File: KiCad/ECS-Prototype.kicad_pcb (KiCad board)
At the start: 2 copper layers, 192.1 x 149.8 mm, 53 parts, among them J1 Connector1, J3 FC68131, J4 FC68131, J5 FC68131, Q1 PN2222A, T1 VB_05-1-12, T2 VB_05-1-12, T3 VB_05-1-12, U3 LT1498IN8, U4 MCP602T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

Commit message: modifications for pcb design: version 3
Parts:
- J3, J4, J5: value FC68131 -> SJ1-3515N; footprint DehneEVSEFootPrints:CLIFF_FC68131 -> ECS-PrototypeFootPrints:CUI_SJ1-3515N
- moved Ref** 1.91 mm to (310.8, 140.9)
- moved ? 1.45 mm to (210.1, 190.4)
- moved ? 1.45 mm to (310.3, 61.4)
- moved C1 1.45 mm to (271.0, 162.4)
- moved C2 1.45 mm to (271.0, 168.7)
- moved C3 1.45 mm to (251.8, 169.7)
- moved D1 1.45 mm to (222.1, 142.7)
- moved D2 1.45 mm to (243.6, 193.4)
- moved D3 1.45 mm to (240.6, 174.4)
- moved D4 1.45 mm to (197.6, 142.7)
- moved D5 1.45 mm to (173.3, 142.7)
- moved D6 1.45 mm to (270.3, 156.7)
- moved G*** 1.45 mm to (203.8, 84.2)
- moved J1 1.45 mm to (159.8, 170.9)
- moved L1 1.45 mm to (250.5, 158.9)
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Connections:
- J3 pad 2: Net-(J3-Pad2) -> CUR_SENS_L1
- J3 pad 5: CUR_SENS_L1 -> (no net)
- J4 pad 2: Net-(J4-Pad2) -> CUR_SENS_L2
- J4 pad 5: CUR_SENS_L2 -> (no net)
- J5 pad 2: Net-(J5-Pad2) -> CUR_SENS_L3
- J5 pad 5: CUR_SENS_L3 -> (no net)
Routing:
- net +5V: track 267.2 -> 348.0 mm, vias 1 -> 6
- net CP: track 184.7 -> 248.7 mm, vias 1 -> 3
- net CURRENT_SENS_L3_READ: track 163.4 -> 220.9 mm, vias 3 -> 4
- net PWM: track 91.2 -> 105.4 mm, vias 1 -> 2
- net VOLTAGE_SENS_L1_READ: track 108.7 -> 115.9 mm, vias 1 -> 2
- net CUR_SENS_L3: track 167.2 -> 173.9 mm
- net +12VDC: track 37.9 -> 44.3 mm, vias 0 -> 2
- net /PP: track 171.9 -> 178.1 mm, vias 2 -> 4
- net DC_RELAY: track 44.2 -> 49.2 mm, vias 1 -> 2
- net CURRENT_SENS_L2_READ: track 125.4 -> 130.3 mm
- net CUR_SENS_L1: track 86.2 -> 90.7 mm
- net +3V3: track 305.7 -> 301.4 mm, vias 1 -> 6
- net CUR_SENS_L2: track 121.7 -> 126.0 mm, vias 1 -> 2
- net Net-(D2-Pad2): track 43.2 -> 47.3 mm, vias 0 -> 2
- net VOLTAGE_SENS_L3_READ: track 193.6 -> 197.5 mm, vias 1 -> 2
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
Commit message: modifications for pcb design version 4: like v3 but with both faces soldering
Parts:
- moved C2 0.46 mm to (271.0, 168.2)
- moved R7 0.13 mm to (276.6, 147.5)
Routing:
- net +5V: track 348.0 -> 331.6 mm, vias 6 -> 1
- net +3V3: track 301.4 -> 317.2 mm, vias 6 -> 1
- net PWM: track 105.4 -> 94.7 mm, vias 2 -> 1
- net +12VDC: track 44.3 -> 38.1 mm, vias 2 -> 0
- net Net-(D2-Pad2): track 47.3 -> 43.8 mm, vias 2 -> 0
- net CUR_SENS_L2: track 126.0 -> 124.0 mm, vias 2 -> 1
- net DC_RELAY: track 49.2 -> 47.2 mm, vias 2 -> 1
- net Net-(R6-Pad2): track 16.3 -> 14.4 mm, vias 2 -> 0
- net CP: track 248.7 -> 246.8 mm, vias 3 -> 1
- net -12VDC: track 21.2 -> 19.7 mm
- net /PP: track 178.1 -> 176.8 mm, vias 4 -> 2
- net CUR_SENS_L3: track 173.9 -> 174.9 mm, vias 2 -> 1
- net MAINS_L1: track 90.6 -> 91.2 mm
- net CUR_SENS_L1: track 90.7 -> 90.6 mm, vias 2 -> 1
- net VOLTAGE_SENS_L3_READ: track 197.5 -> 197.4 mm, vias 2 -> 1
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
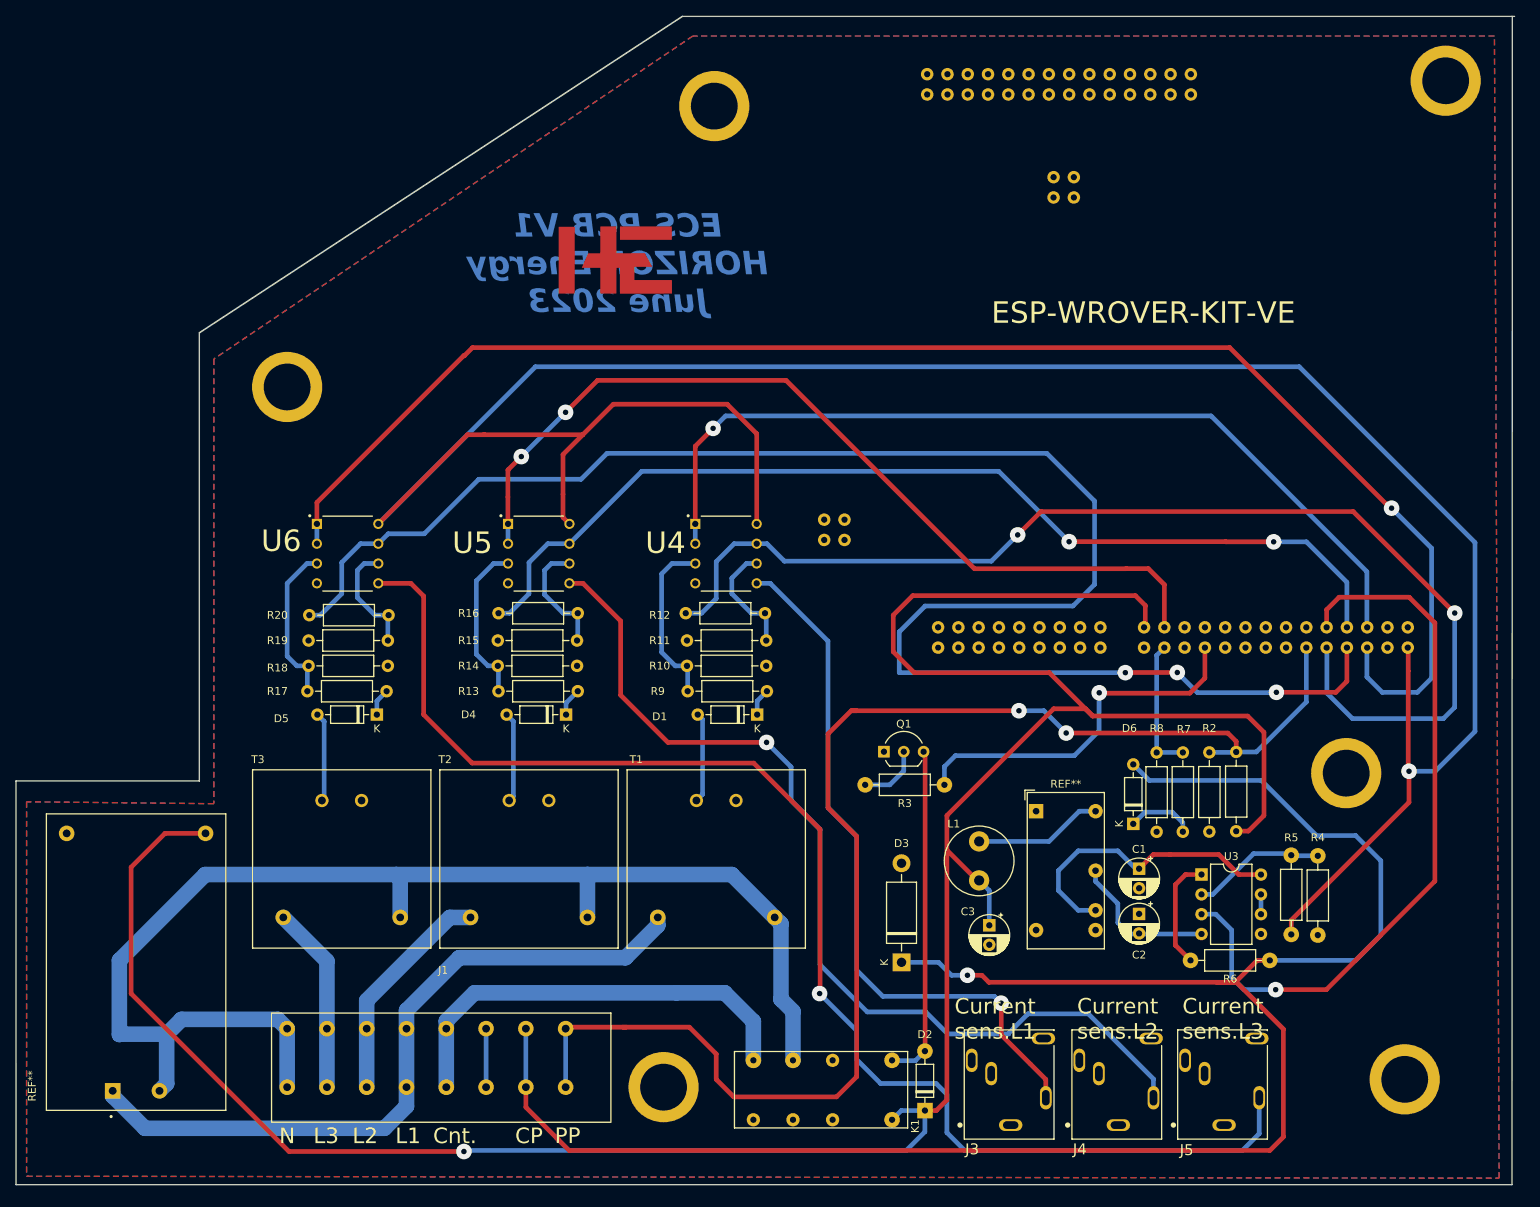
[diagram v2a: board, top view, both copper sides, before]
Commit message: modifications for pcb design v6: like v4 but with modified jack and 0.8 vias
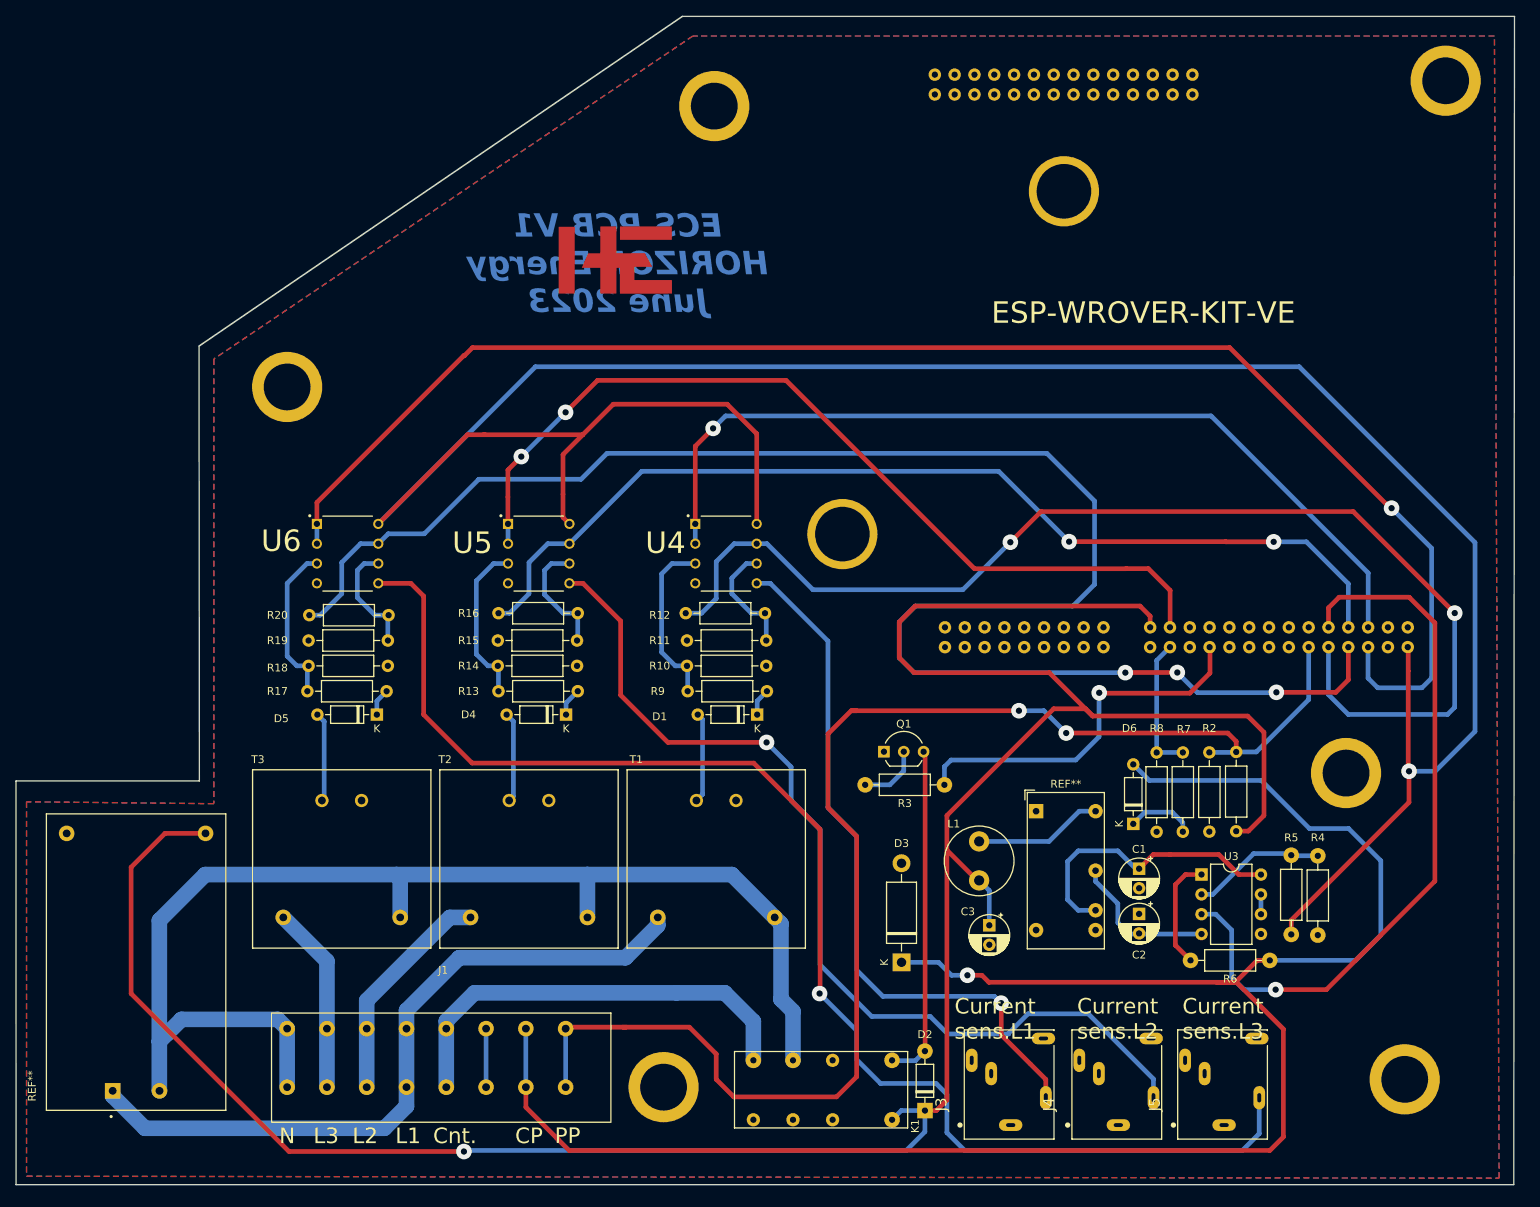
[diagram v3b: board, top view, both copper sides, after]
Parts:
- added ?: , , F.Cu at (233.5, 118.5)
- added ?: , , F.Cu at (263.0, 75.1)
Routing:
- net MAINS_N: track 168.7 -> 161.5 mm
- net +5V: track 331.6 -> 328.4 mm
- net CURRENT_SENS_L1_READ: track 150.5 -> 152.8 mm
- net +12VDC: track 38.1 -> 37.2 mm
- net DC_RELAY: track 47.2 -> 48.0 mm
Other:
- outline, holes or cut-outs redrawn

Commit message: modifications for pcb design v7: like v5 but with modified jack and 0.8mm vias
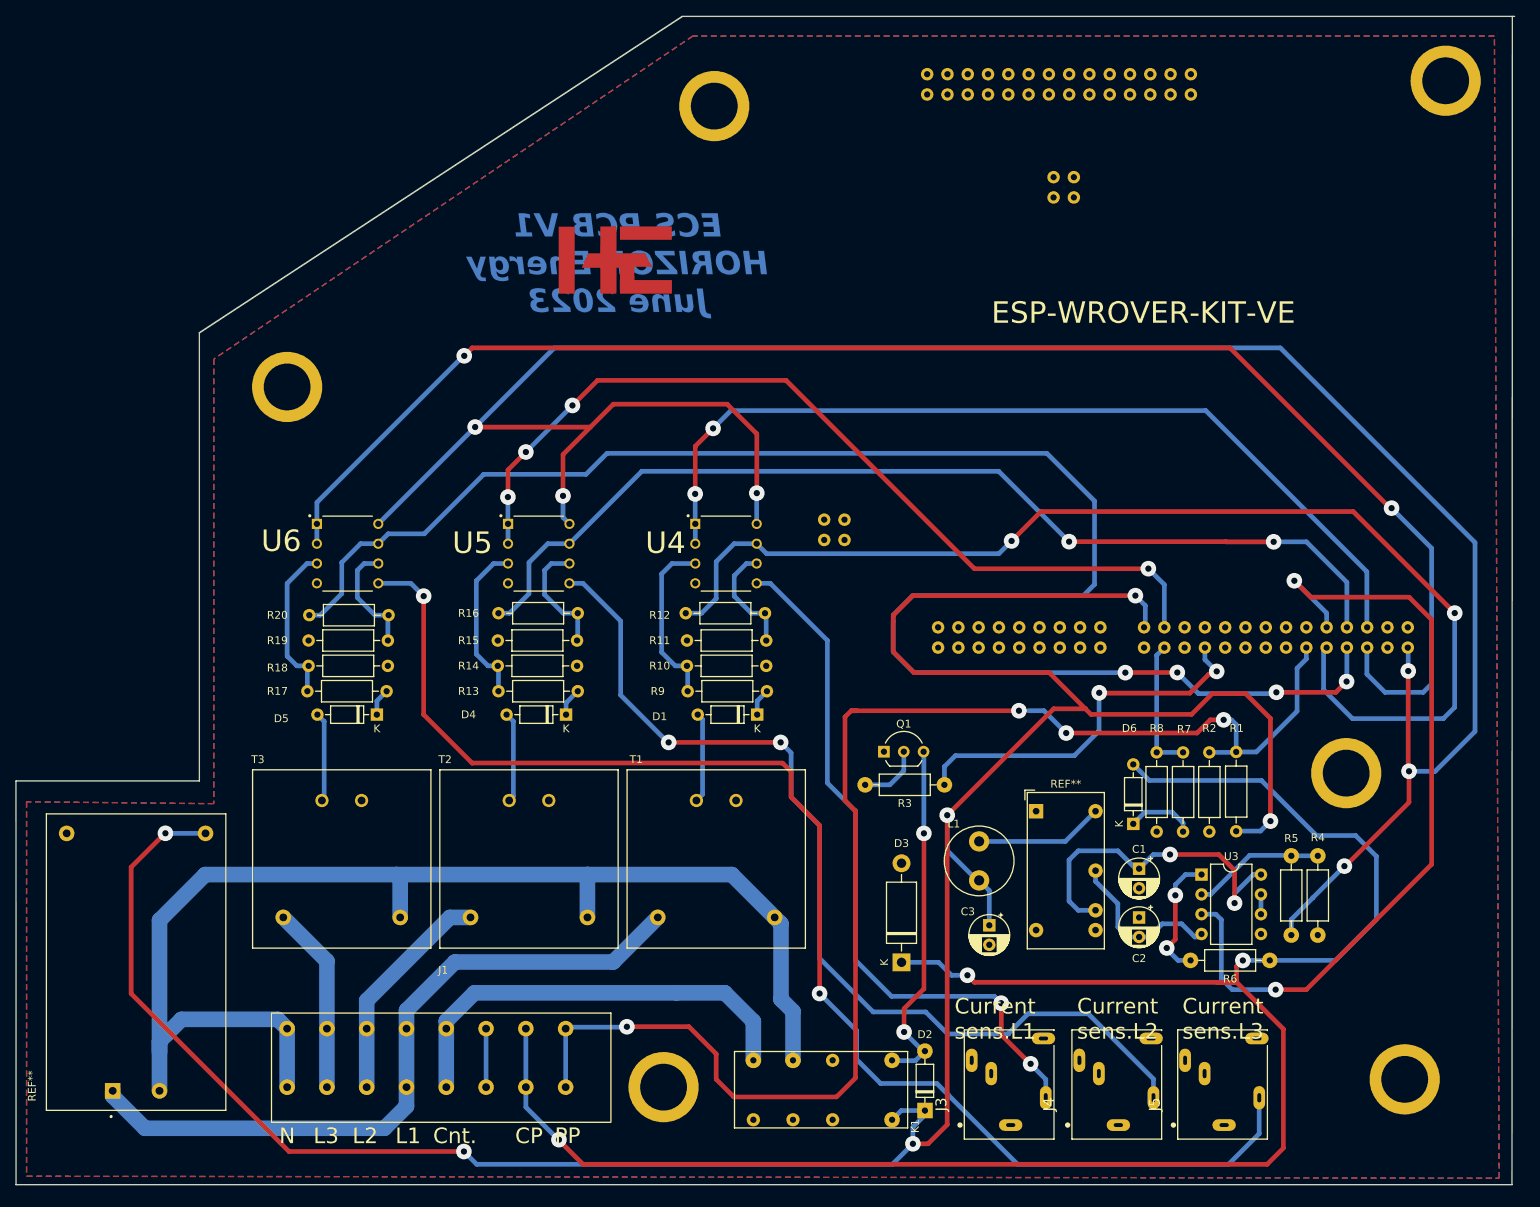
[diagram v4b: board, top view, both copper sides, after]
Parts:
- removed the ? at (233.5, 118.5)
- removed the ? at (263.0, 75.1)
- moved C2 0.46 mm to (271.0, 168.7)
- moved R5 0.08 mm to (290.5, 160.8)
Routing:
- net +5V: track 328.4 -> 347.2 mm, vias 1 -> 6
- net +3V3: track 317.2 -> 303.0 mm, vias 1 -> 6
- net PWM: track 94.4 -> 103.5 mm, vias 1 -> 2
- net +12VDC: track 37.2 -> 43.2 mm, vias 0 -> 2
- net CURRENT_SENS_L1_READ: track 152.8 -> 150.1 mm
- net Net-(D2-Pad2): track 43.8 -> 45.9 mm, vias 0 -> 2
- net Net-(R6-Pad2): track 14.4 -> 16.3 mm, vias 0 -> 2
- net CURRENT_SENS_L3_READ: track 220.7 -> 222.3 mm, vias 3 -> 4
- net -12VDC: track 19.7 -> 21.2 mm
- net MAINS_N: track 161.5 -> 162.9 mm
- net DC_RELAY: track 48.0 -> 49.2 mm, vias 1 -> 2
- net /PP: track 177.0 -> 175.9 mm, vias 2 -> 4
- net CP: track 246.8 -> 247.9 mm, vias 1 -> 3
- net CUR_SENS_L3: track 174.9 -> 175.6 mm, vias 1 -> 2
- net CUR_SENS_L2: track 124.0 -> 124.7 mm, vias 1 -> 2
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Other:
- outline, holes or cut-outs redrawn
